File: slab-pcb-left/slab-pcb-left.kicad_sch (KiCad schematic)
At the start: 125 parts, among them J1 MagnetR, J2 MagnetL, J3 TRRS_R, J4 TRRS_L, J5 SSD1306, J6 Conn_01x06, Q1 MMBT3906, SW1 RotaryEncoder, U1 Seeeduino Xiao rp2040, U2 PCA9555PW, U3 PCA9555PW, U4 ADS1110, U5 SN74AHCT125PWR

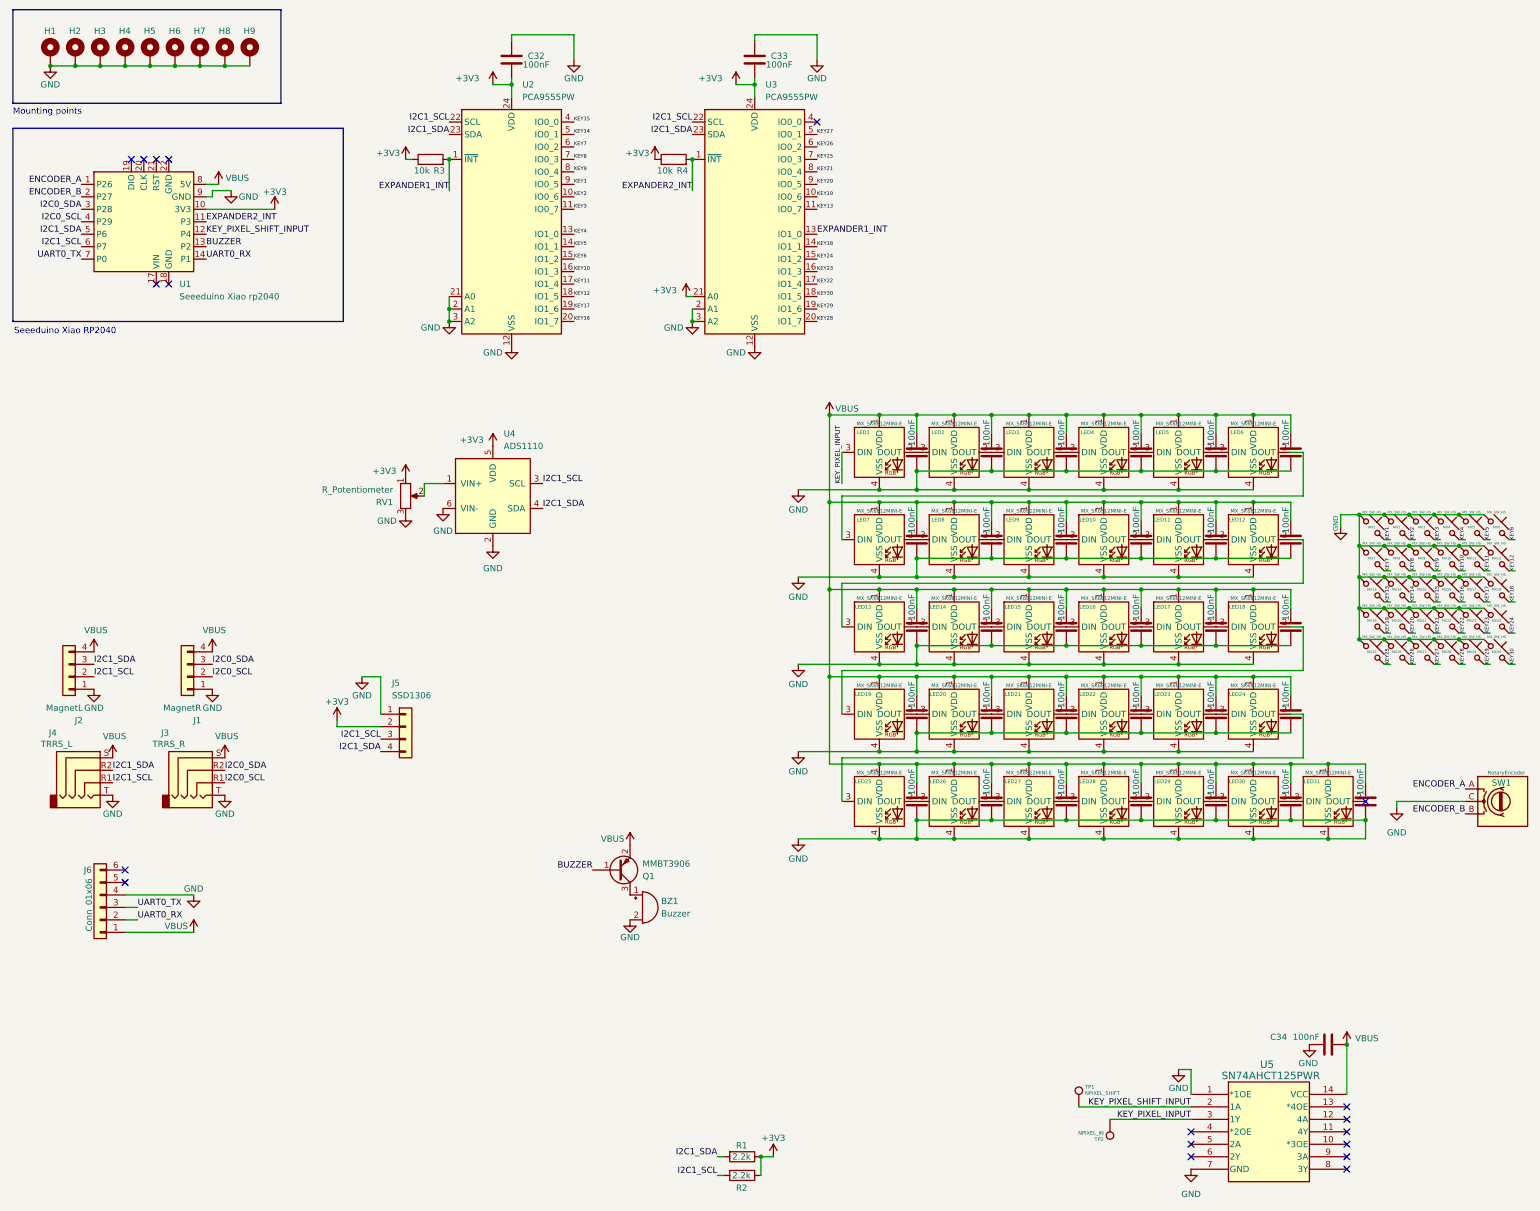
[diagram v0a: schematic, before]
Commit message: fix: inconsistent design
all modules now share the same design - with updated footprints to
support both choc+mx PCB mounting holes.
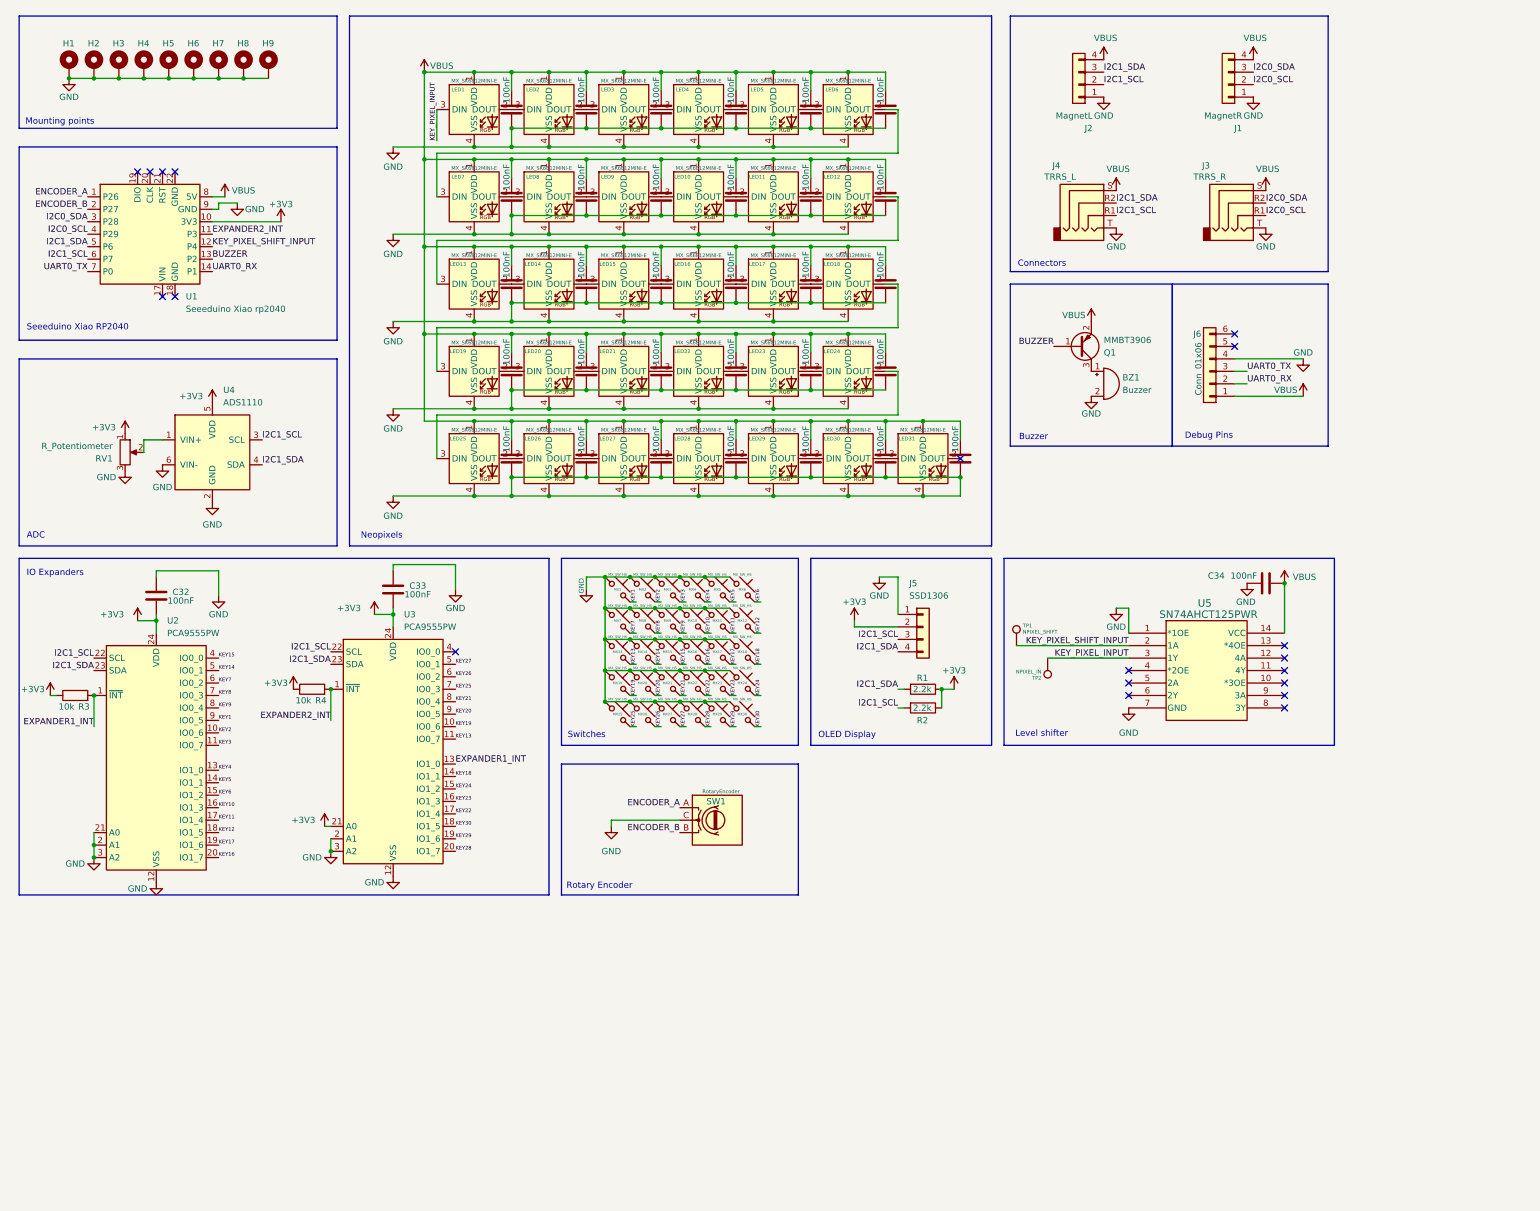
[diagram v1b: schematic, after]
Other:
- note added: "ADC"
- note added: "Buzzer"
- note added: "Connectors"
- note added: "Debug Pins"
- note added: "IO Expanders"
- note added: "Level shifter"
- note added: "Neopixels"
- note added: "OLED Display"
- note added: "Rotary Encoder"
- note added: "Switches"
- company: (none) -> Edward Hesketh
- title: (none) -> Slab Keyboard - Left Module
- moved on the sheet: BZ1, C32, C33, C34, H1, H2, H3, H4, H5, H6, H7, H8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

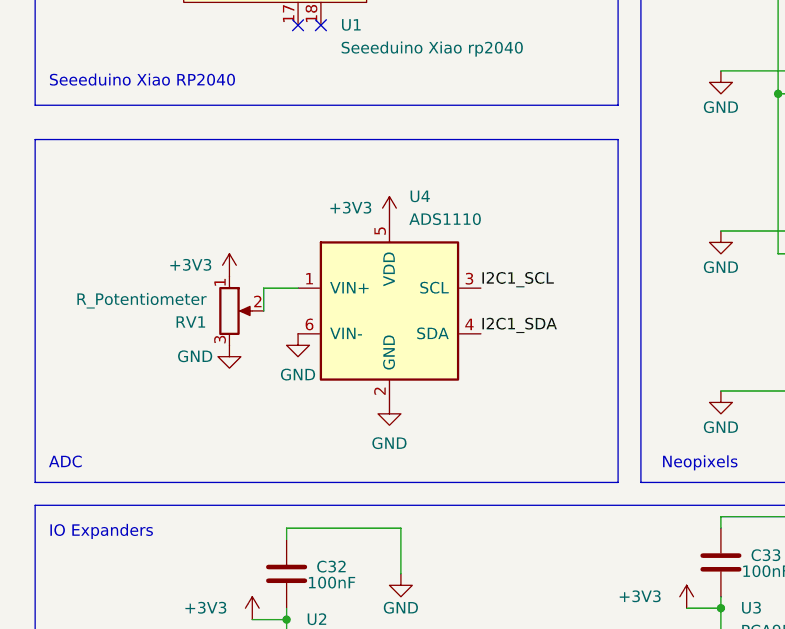
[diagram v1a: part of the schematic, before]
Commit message: fix: add voltage divider to potentiometer
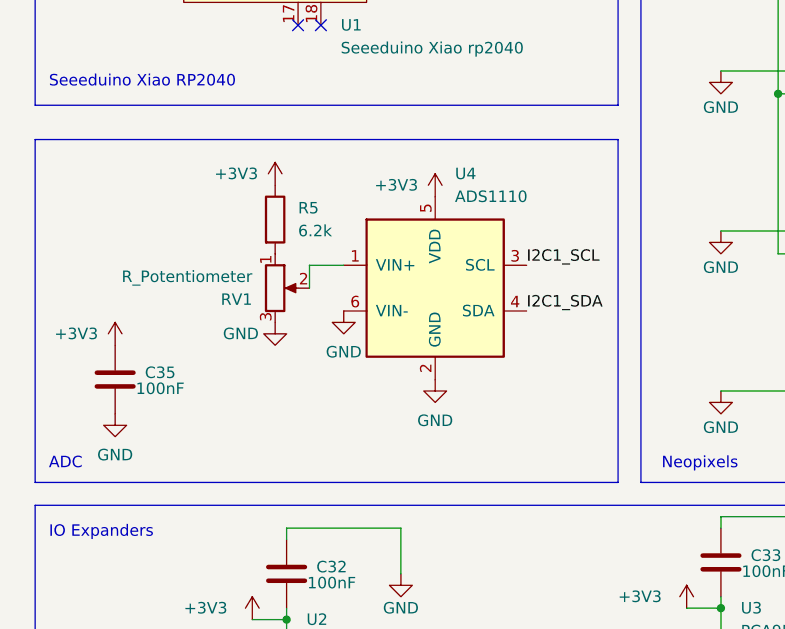
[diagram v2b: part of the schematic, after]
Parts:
- added C35: 100nF, Capacitor_SMD:C_0603_1608Metric_Pad1.08x0.95mm_HandSolder, symbol Device:C
- added R5: 6.2k, Resistor_SMD:R_0603_1608Metric_Pad0.98x0.95mm_HandSolder, symbol Device:R
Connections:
- net +3V3: now also C35.2, R5.1; no longer RV1.1
- net GND: now also C35.1
- new net: R5.2, RV1.1
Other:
- moved on the sheet: RV1, U4

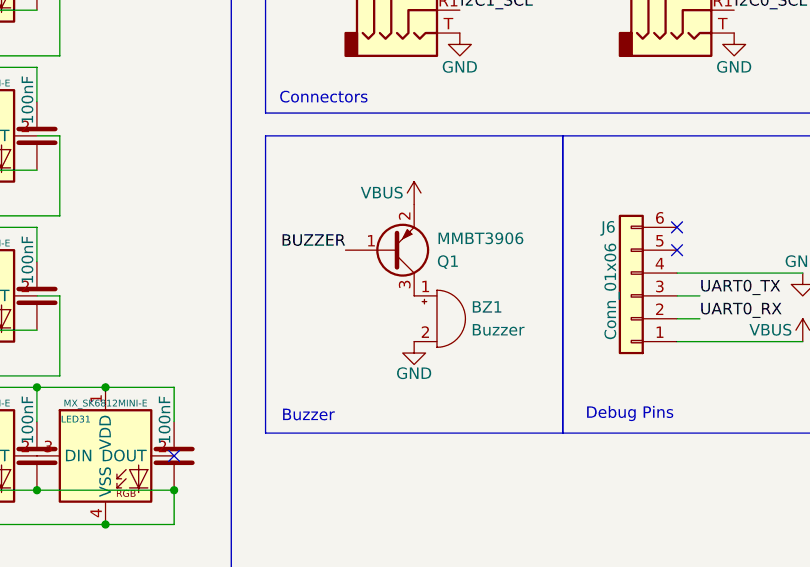
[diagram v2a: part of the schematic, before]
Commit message: feat: use slots instead of overlapped drill hits
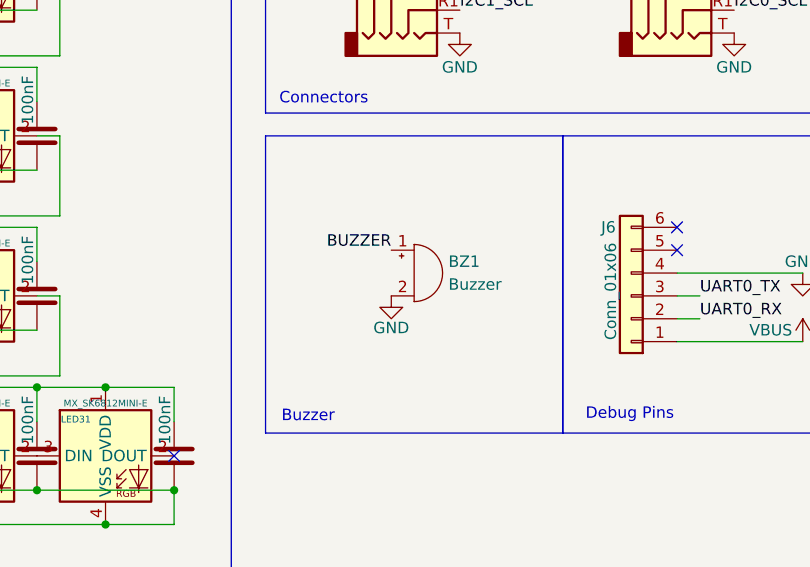
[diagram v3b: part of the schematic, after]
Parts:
- removed Q1: MMBT3906, Package_TO_SOT_SMD:SOT-23, symbol Transistor_BJT:MMBT3906
- BZ1: footprint Buzzer_Beeper:MagneticBuzzer_CUI_CMT-8504-100-SMT -> CustomFootprints:buzzer
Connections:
- net BUZZER: now also BZ1.1 (+)
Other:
- moved on the sheet: BZ1
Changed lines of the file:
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@@
 	)
 	(label "BUZZER"
-		(at 226.06 82.55 180)
+		(at 231.14 82.55 180)
 		(fields_autoplaced yes)
 		(effects
@@
 	)
 	(symbol
-		(lib_id "Transistor_BJT:MMBT3906")
-		(at 231.14 82.55 0)
-		(mirror x)
-		(unit 1)
-		(exclude_from_sim no)
-		(in_bom yes)
-		(on_board yes)
-		(dnp no)
-		(property "Reference" "Q1"
-			(at 236.22 83.8201 0)
-			(effects
-				(font
-					(size 1.27 1.27)
-				)
-				(justify left)
-			)
-		)
-		(property "Value" "MMBT3906"
-			(at 236.22 81.2801 0)
-			(effects
-				(font
-					(size 1.27 1.27)
-				)
-				(justify left)
-			)
-		)
-		(property "Footprint" "Package_TO_SOT_SMD:SOT-23"
-			(at 236.22 80.645 0)
-			(effects
-				(font
-					(size 1.27 1.27)
-					(italic yes)
-				)
-				(justify left)
-				(hide yes)
-			)
-		)
-		(property "Datasheet" "https://www.onsemi.com/pdf/datasheet/pzt3906-d.pdf"
-			(at 231.14 82.55 0)
-			(effects
-				(font
-					(size 1.27 1.27)
-				)
-				(justify left)
-				(hide yes)
-			)
-		)
-		(property "Description" "-0.2A Ic, -40V Vce, Small Signal PNP Transistor, SOT-23"
-			(at 231.14 82.55 0)
-			(effects
-				(font
-					(size 1.27 1.27)
-				)
-				(hide yes)
-			)
-		)
-		(pin "1"
-		)
-		(pin "3"
-		)
-		(pin "2"
-		)
-		(instances
-			(project "slab-pcb-left"
-				(path "/e2e6982a-5531-4cb6-b818-e99b542930a3"
-					(reference "Q1")
-					(unit 1)
-				)
-			)
-		)
-	)
-	(symbol
 		(lib_id "power:+3V3")
 		(at 41.91 90.17 0)
@@
 	)
 	(symbol
-		(lib_id "power:VBUS")
-		(at 233.68 77.47 0)
-		(unit 1)
-		(exclude_from_sim no)
-		(in_bom yes)
-		(on_board yes)
-		(dnp no)
-		(property "Reference" "#PWR09"
-			(at 233.68 81.28 0)
-			(effects
-				(font
-					(size 1.27 1.27)
-				)
-				(hide yes)
-			)
-		)
-		(property "Value" "VBUS"
-			(at 230.124 76.2 0)
-			(effects
-				(font
-					(size 1.27 1.27)
-				)
-			)
-		)
-		(property "Footprint" ""
-			(at 233.68 77.47 0)
-			(effects
-				(font
-					(size 1.27 1.27)
-				)
-				(hide yes)
-			)
-		)
-		(property "Datasheet" ""
-			(at 233.68 77.47 0)
-			(effects
-				(font
-					(size 1.27 1.27)
-				)
-				(hide yes)
-			)
-		)
-		(property "Description" "Power symbol creates a global label with name \"VBUS\""
-			(at 233.68 77.47 0)
-			(effects
-				(font
-					(size 1.27 1.27)
-				)
-				(hide yes)
-			)
-		)
-		(pin "1"
-		)
-		(instances
-			(project "slab-pcb-left"
-				(path "/e2e6982a-5531-4cb6-b818-e99b542930a3"
-					(reference "#PWR09")
-					(unit 1)
-				)
-			)
-		)
-	)
-	(symbol
 		(lib_id "power:+3V3")
 		(at 71.12 152.4 0)
@@
 	(symbol
 		(lib_id "Device:Buzzer")
-		(at 236.22 90.17 0)
+		(at 233.68 85.09 0)
 		(unit 1)
 		(exclude_from_sim no)
@@
 		(fields_autoplaced yes)
 		(property "Reference" "BZ1"
-			(at 240.03 88.8999 0)
+			(at 237.49 83.8199 0)
 			(effects
 				(font
@@
 		)
 		(property "Value" "Buzzer"
-			(at 240.03 91.4399 0)
+			(at 237.49 86.3599 0)
 			(effects
 				(font
@@
 			)
 		)
-		(property "Footprint" "Buzzer_Beeper:MagneticBuzzer_CUI_CMT-8504-100-SMT"
-			(at 235.585 87.63 90)
+		(property "Footprint" "CustomFootprints:buzzer"
+			(at 233.045 82.55 90)
 			(effects
 				(font
@@
 		)
 		(property "Datasheet" "~"
-			(at 235.585 87.63 90)
+			(at 233.045 82.55 90)
 			(effects
 				(font
@@
 		)
 		(property "Description" "Buzzer, polarized"
-			(at 236.22 90.17 0)
+			(at 233.68 85.09 0)
 			(effects
 				(font
@@
 	(symbol
 		(lib_id "power:GND")
-		(at 233.68 92.71 0)
+		(at 231.14 87.63 0)
 		(unit 1)
 		(exclude_from_sim no)
@@
 		(dnp no)
 		(property "Reference" "#PWR08"
-			(at 233.68 99.06 0)
+			(at 231.14 93.98 0)
 			(effects
 				(font
@@
 		)
 		(property "Value" "GND"
-			(at 233.68 96.266 0)
+			(at 231.14 91.186 0)
 			(effects
 				(font
@@
 		)
 		(property "Footprint" ""
-			(at 233.68 92.71 0)
+			(at 231.14 87.63 0)
 			(effects
 				(font
@@
 		)
 		(property "Datasheet" ""
-			(at 233.68 92.71 0)
+			(at 231.14 87.63 0)
 			(effects
 				(font
@@
 		)
 		(property "Description" ""
-			(at 233.68 92.71 0)
+			(at 231.14 87.63 0)
 			(effects
 				(font

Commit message: feat: add User.6 as printable layout helper
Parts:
- BZ1: LCSC (none) -> C94599
- C1, C10, C11, C12, C13, C14, C15, C16, C17, C18, C19, C2, C20, C21, C22, C23, C24, C25, C26, C27, C28, C29, C3, C30, C31, C32, C33, C34, C35, C4, C5, C6, C7, C8, C9: LCSC (none) -> C14663
- J3, J4: LCSC (none) -> C95562
- J5: LCSC (none) -> C5248081
- LED1, LED10, LED11, LED12, LED13, LED14, LED15, LED16, LED17, LED18, LED19, LED2, LED20, LED21, LED22, LED23, LED24, LED25, LED26, LED27, LED28, LED29, LED3, LED30, LED31, LED4, LED5, LED6, LED7, LED8, LED9: LCSC (none) -> C5149201
- MX1, MX10, MX11, MX12, MX13, MX14, MX15, MX16, MX17, MX18, MX19, MX2, MX20, MX21, MX22, MX23, MX24, MX25, MX26, MX27, MX28, MX29, MX3, MX30, MX4, MX5, MX6, MX7, MX8, MX9: LCSC (none) -> C41430893
- R1, R2: LCSC (none) -> C4190
- R3, R4: LCSC (none) -> C25804
- R5: LCSC (none) -> C2907054
- RV1: LCSC (none) -> C470640
- SW1: LCSC (none) -> C351235
- U2, U3: LCSC (none) -> C128392
- U4: LCSC (none) -> C22471993
- U5: LCSC (none) -> C36365

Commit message: feat: start on v4, updated: right-hand schematic
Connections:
- net EXPANDER1_INT: now also U1.14 (P1); no longer U3.13 (IO1_0)
- net UART0_RX: no longer U1.14 (P1)
- net UART0_TX: no longer U1.7 (P0)
- no-connect marks 19 -> 21
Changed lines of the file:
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@@
 	)
 	(no_connect
+		(at 104.14 167.64)
+	)
+	(no_connect
 		(at 241.3 151.13)
 	)
@@
 	)
 	(no_connect
+		(at 29.21 67.31)
+	)
+	(no_connect
 		(at 273.05 156.21)
 	)
@@
 		)
 	)
-	(label "KEY_PIXEL_SHIFT_INPUT"
-		(at 241.3 143.51 180)
+	(label "EXPANDER1_INT"
+		(at 54.61 67.31 0)
 		(fields_autoplaced yes)
 		(effects
@@
 				(size 1.27 1.27)
 			)
-			(justify right bottom)
+			(justify left bottom)
 		)
 	)
-	(label "I2C1_SCL"
-		(at 236.22 29.21 0)
+	(label "KEY_PIXEL_SHIFT_INPUT"
+		(at 241.3 143.51 180)
 		(fields_autoplaced yes)
 		(effects
@@
 				(size 1.27 1.27)
 			)
-			(justify left bottom)
+			(justify right bottom)
 		)
 	)
-	(label "UART0_TX"
-		(at 29.21 67.31 180)
+	(label "I2C1_SCL"
+		(at 236.22 29.21 0)
 		(fields_autoplaced yes)
 		(effects
@@
 				(size 1.27 1.27)
 			)
-			(justify right bottom)
+			(justify left bottom)
 		)
 	)
@@
 		)
 	)
-	(label "UART0_RX"
-		(at 54.61 67.31 0)
-		(fields_autoplaced yes)
-		(effects
-			(font
-				(size 1.27 1.27)
-			)
-			(justify left bottom)
-		)
-	)
 	(label "I2C1_SCL"
 		(at 78.74 144.78 180)
@@
 			)
 			(justify left bottom)
-		)
-	)
-	(label "EXPANDER1_INT"
-		(at 104.14 167.64 0)
-		(fields_autoplaced yes)
-		(effects
-			(font
-				(size 1.27 1.27)
-			)
-			(justify left bottom)
